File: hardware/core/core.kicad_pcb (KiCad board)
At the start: 4 copper layers, 31.3 x 67.7 mm, 32 parts, among them J17 PROG, J18 USB_C_Receptacle_USB2.0_14P, J5 TO_NEXT, J7 TO_NEXT, J8 Conn_02x09_Odd_Even, SW1 RESET, SW2 BOOT, U10 SN74AHCT1G14DCKR, U19 ESP32-S3-MINI-1, U20 AP2112K-3.3TRG1, U21 SN65HVD230DR

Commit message: fix(hardware): finalize core layout and USB constraints
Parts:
- removed J18: USB_C_Receptacle_USB2.0_14P, SpaghettiLAB2:USB-C-SMD_TYPEC-324G-BCP24
- added USBC1: TYPE-C-31-M-12, SpaghettiLAB:USB-C_SMD-TYPE-C-31-M-12_1, F.Cu at (71.7, 128.7)
- moved J5 5.00 mm to (95.8, 82.9)
- moved J7 5.00 mm to (95.7, 130.5)
- moved J8 0.43 mm to (78.7, 69.8)
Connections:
- SW1 pad 2: Net-(U19-EN) -> unconnected-(SW1-Pad2)
- SW1 pad 3: unconnected-(SW1-Pad3) -> Net-(U19-EN)
- SW2 pad 2: Net-(U19-IO0) -> unconnected-(SW2-Pad2)
- SW2 pad 3: unconnected-(SW2-Pad3) -> Net-(U19-IO0)
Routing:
- net Net-(J18-CC2): track 12.0 -> 2.47 mm, vias 2 -> 1
- net Net-(U19-EN): track 25.3 -> 33.5 mm
- net Net-(USBC1-DN1): track 15.9 -> 10.0 mm
- net Net-(USBC1-CC2): track 3.65 -> 9.38 mm, vias 0 -> 2
- net Net-(USBC1-DP1): track 13.0 -> 8.60 mm
- net GND: track 14.1 -> 9.81 mm, vias 23 -> 21
- net VBUS: track 10.3 -> 7.00 mm, vias 6 -> 2
- net Net-(USBC1-CC1): track 0.00 -> 2.04 mm, vias 0 -> 1
- net CORE_CANL: track 42.1 -> 40.4 mm
- net CORE_CANH: track 37.4 -> 36.2 mm
- net Net-(LED2-DIN): track 2.24 -> 2.96 mm
- net LED_DATA: track 27.9 -> 27.3 mm
- net 5V: track 22.4 -> 23.0 mm
- net VCORE: vias 7 -> 8
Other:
- board text added: "REV B"
- board text removed: "1"
- board text removed: "1 to 5"
- board text removed: "2"
- board text removed: "3"
- board text removed: "4"
- board text removed: "5"
- board text removed: "5v"
- board text removed: "BOARD"
- board text removed: "CORE"
- board text removed: "REV A"
- board text removed: "can_H"
- board text removed: "can_L"
- board text removed: "gnd"
- board text removed: "term"

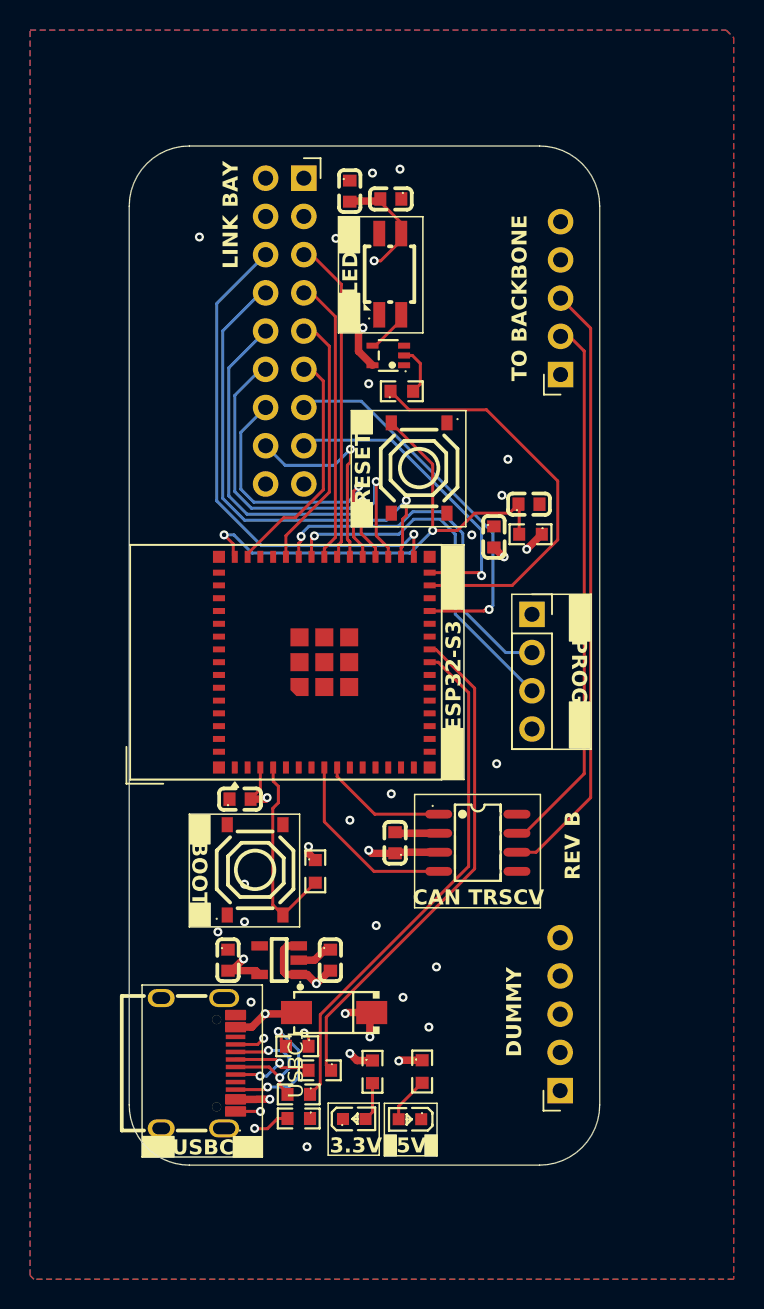
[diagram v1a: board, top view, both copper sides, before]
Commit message: Added oval style silkscreen
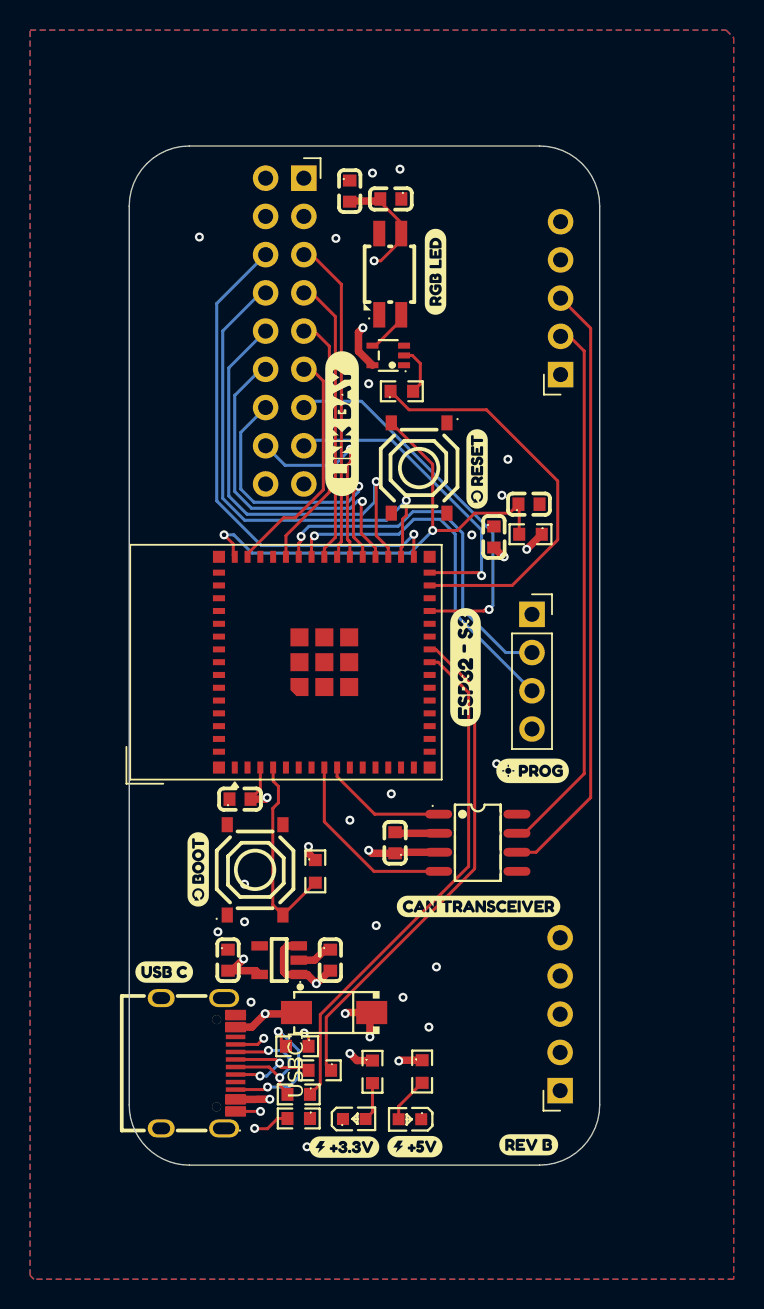
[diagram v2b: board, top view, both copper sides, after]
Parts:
- added kobee-studio-6AA83D3C: Kobee Studio, kobee-studio-6AA83D3C, F.Cu at (81.2, 86.2)
- added kobee-studio-6AA83E19: Kobee Studio, kobee-studio-6AA83D3C, F.Cu at (90.2, 89.2)
- added kobee-studio-6AA83E1F: Kobee Studio, kobee-studio-6AA83D3C, F.Cu at (87.4, 76.1)
- added kobee-studio-6AA83E37: Kobee Studio, kobee-studio-6AA83D3C, F.Cu at (71.7, 115.8)
- added kobee-studio-6AA83E5B: Kobee Studio, kobee-studio-6AA83D3C, F.Cu at (90.3, 118.2)
- added kobee-studio-6AA83E8C: Kobee Studio, kobee-studio-6AA83D3C, F.Cu at (93.6, 134.1)
- added kobee-studio-6AA83EC3: Kobee Studio, kobee-studio-6AA83D3C, F.Cu at (86.1, 134.2)
- added kobee-studio-6AA83ED5: Kobee Studio, kobee-studio-6AA83D3C, F.Cu at (81.4, 134.2)
- added kobee-studio-6AA83EFB: Kobee Studio, kobee-studio-6AA83D3C, F.Cu at (69.4, 122.6)
- added kobee-studio-6AA83FBE: Kobee Studio, kobee-studio-6AA83D3C, F.Cu at (93.9, 109.2)
- added kobee-studio-6AA83FED: Kobee Studio, kobee-studio-6AA83D3C, F.Cu at (89.4, 102.3)
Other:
- board text removed: "3.3V"
- board text removed: "5V"
- board text removed: "BOOT"
- board text removed: "CAN TRSCV"
- board text removed: "DUMMY"
- board text removed: "ESP32-S3"
- board text removed: "LED"
- board text removed: "LINK BAY"
- board text removed: "PROG"
- board text removed: "RESET"
- board text removed: "REV B"
- board text removed: "TO BACKBONE"
- board text removed: "USBC"
